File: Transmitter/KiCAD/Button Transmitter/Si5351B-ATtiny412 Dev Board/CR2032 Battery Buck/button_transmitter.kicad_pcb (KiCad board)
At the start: 2 copper layers, 24.4 x 24.4 mm, 37 parts, among them J1 1.27mm Pogo Pads, J2 Conn_Coaxial, Q1 MMUN2238LT1G, U1 ATtiny412-SS, U2 Si5351B-B-GM1, U3 TLV62568DRL, Y1 25MHz

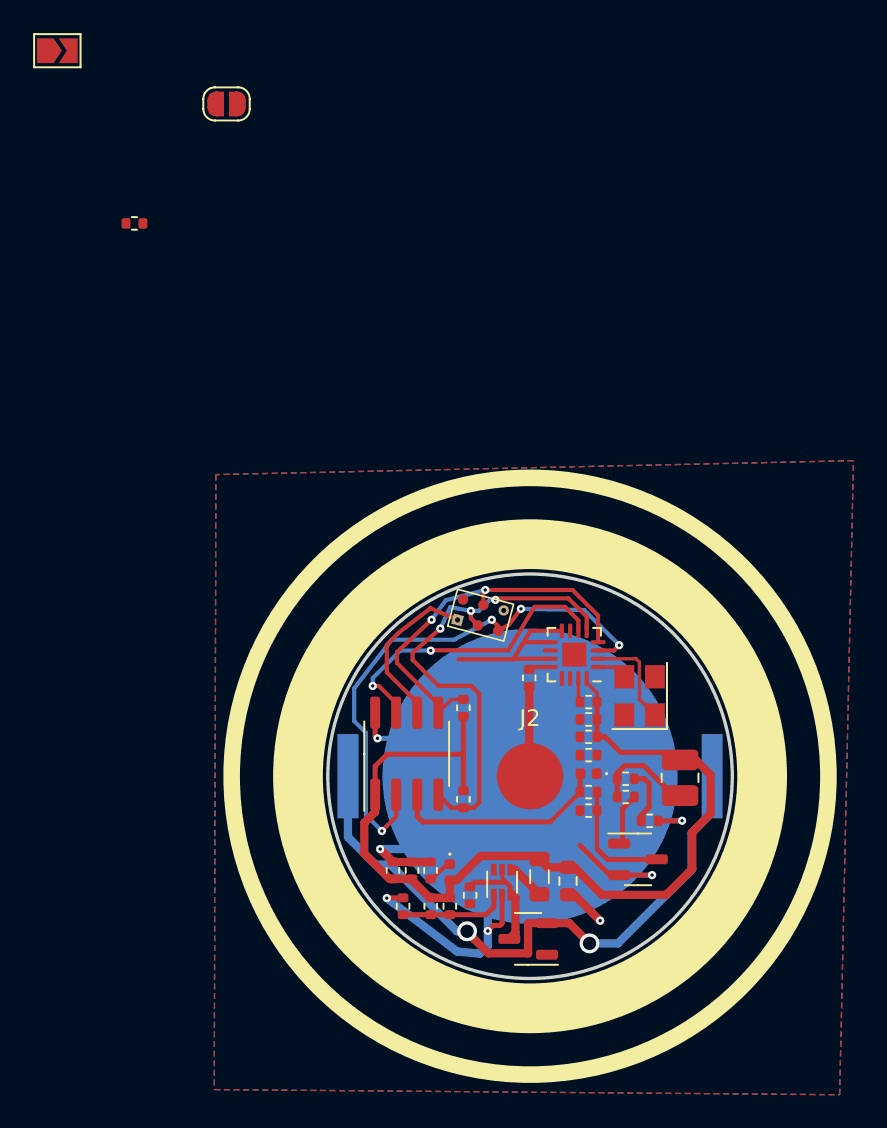
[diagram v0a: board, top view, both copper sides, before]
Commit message: Finished CR2032 layout
I realize now that I should replace the buck converter with a boost converter, going to make a modified version that uses that instead
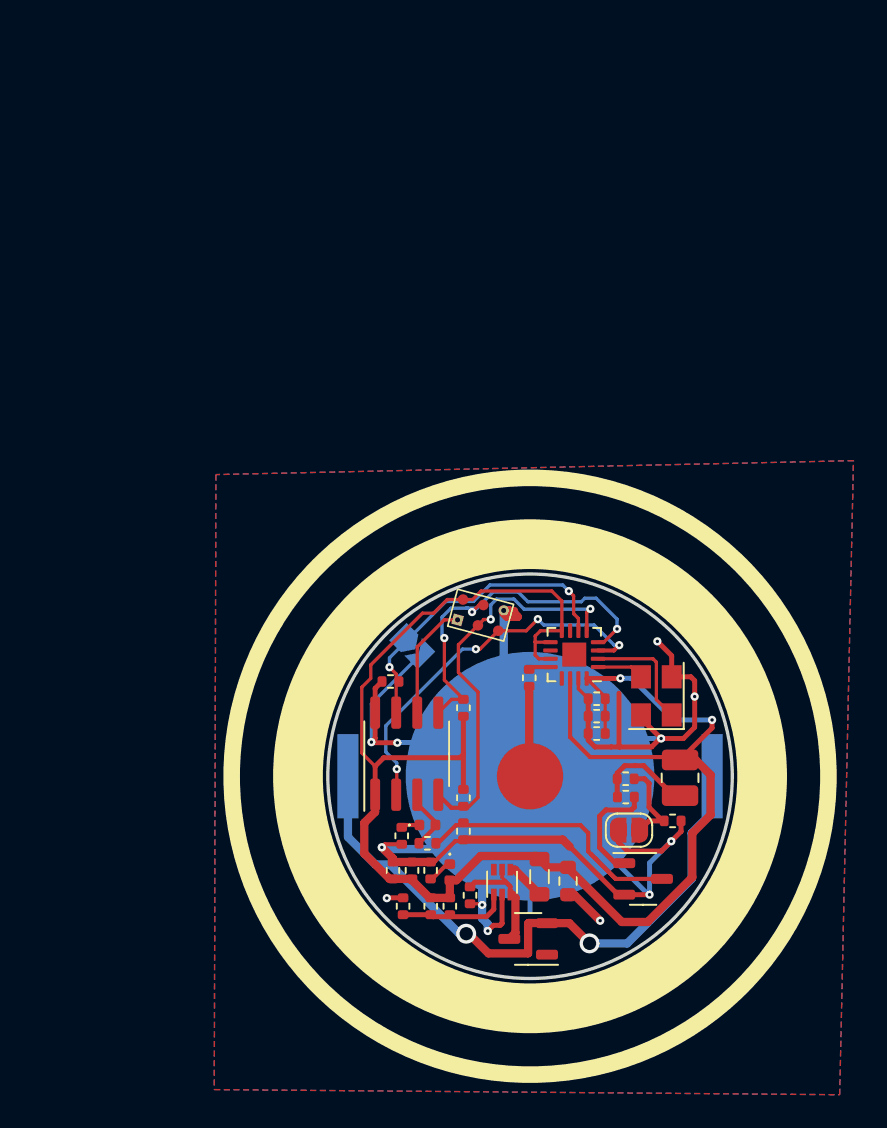
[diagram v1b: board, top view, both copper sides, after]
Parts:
- C10: value 4.7uF -> 10uF
- D2: value CM1213A-01SO -> LS0504EVT233
- JP1: moved to B.Cu
- R7: value 5M -> 1M
- moved BZ1 50.1 mm to (81.6, 107.2), turned to 180 degrees
- moved JP1 41.8 mm to (68.5, 96.1), turned to -45 degrees
- moved C6 31.7 mm to (67.2, 98.2)
- moved R8 12.3 mm to (67.9, 107.5), turned to -90 degrees
- moved D1 10.2 mm to (69.4, 106.9), turned to 0 degrees
- moved R6 10.2 mm to (69.4, 108.0)
- moved R7 7.65 mm to (71.6, 107.2), turned to -90 degrees
- moved C5 2.35 mm to (79.6, 99.2)
- moved R4 1.38 mm to (84.2, 106.6)
- moved Q1 1.22 mm to (82.4, 110.1)
- moved Y1 1.01 mm to (83.2, 99.1)
- moved C4 0.98 mm to (79.6, 100.3)
- moved C3 0.98 mm to (79.6, 101.3)
- moved R1 0.09 mm to (71.6, 105.2)
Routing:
- net GND: track 87.3 -> 141.9 mm, vias 7 -> 12
- net +3V3: track 68.9 -> 103.6 mm, vias 0 -> 2
- net Net-(Q1-G): track 7.31 -> 18.3 mm
- net /MCU_DAC0: track 32.9 -> 23.3 mm
- net Net-(D1-A): track 13.1 -> 3.80 mm
- net /MCU_SDA: track 29.4 -> 24.0 mm, vias 3 -> 2
- net Net-(Q1-D): track 2.70 -> 6.70 mm
- net /MCU_UPDI: track 10.1 -> 7.67 mm
- net Net-(BZ1-+): track 3.47 -> 5.41 mm
- net Net-(D1-K): track 0.00 -> 1.12 mm
- net /~{TX_EN}: track 18.4 -> 19.5 mm
- net Net-(U2-XA): track 1.82 -> 2.83 mm
- net Net-(U2-XB): track 6.16 -> 7.17 mm
- net /MCU_SCL: track 23.3 -> 23.7 mm, vias 2 -> 3
